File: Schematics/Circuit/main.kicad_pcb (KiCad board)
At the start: 2 copper layers, 58.9 x 59 mm, 103 parts, among them IC1 NCP1117ST33T3G, IC2 NCP1117ST50T3G, IC3 ATMEGA2560-A, IC4 RFM69HW, J1 Conn_01x03, J10 Conn_01x04, J11 Conn_01x04, J12 Conn_01x01, J13 Conn_01x02, J14 Conn_01x02, J15 Conn_01x02, J16 Conn_01x02, J2 Conn_01x07, J3 Conn_01x07, J4 Conn_01x07, J5 Conn_01x07, J6 Conn_01x07, J7 Conn_01x05, J8 Conn_02x05_Counter_Clockwise, J9 Conn_01x06, K1 HESOP1, K2 HESOP1, P1 CONN_2, P10 CONN_2, P11 CONN_2, P12 CONN_2, P13 CONN_2, P14 CONN_2, P15 CONN_2, P16 CONN_2, P17 CONN_2, P18 CONN_3X2, P19 CONN_O2, P2 CONN_2, P20 CONN_2, P21 CONN_2, P3 CONN_2, P4 CONN_2, P5 CONN_2, P6 CONN_2, P7 CONN_2, P8 CONN_2, P9 CONN_2, Q1 BSS138, Q2 BSS138, Q3 BSS138, Q4 BSS138, Q5 BSS138, Q6 BSS138, SW1 SW_DIP_x01, SW7 SW_DIP_x01

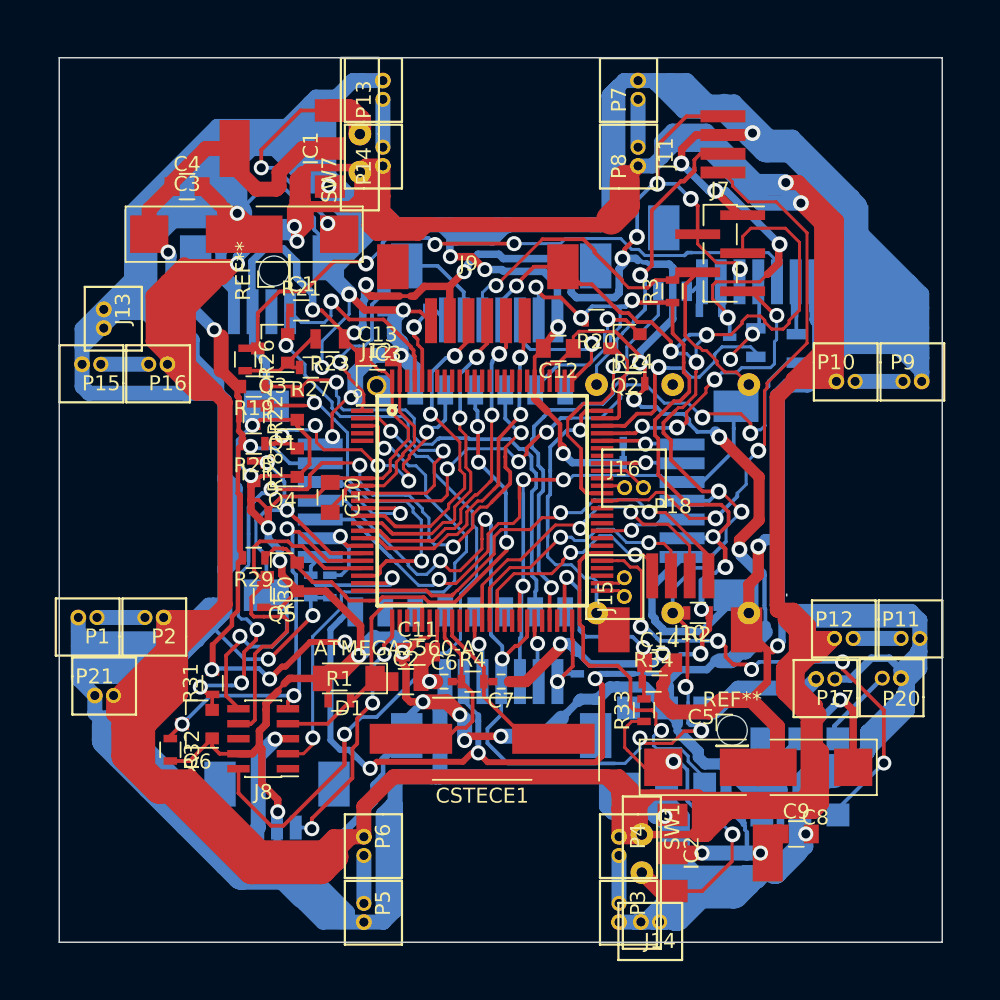
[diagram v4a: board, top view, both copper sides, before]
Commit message: Add UV and Gamma detection, fix main pcb
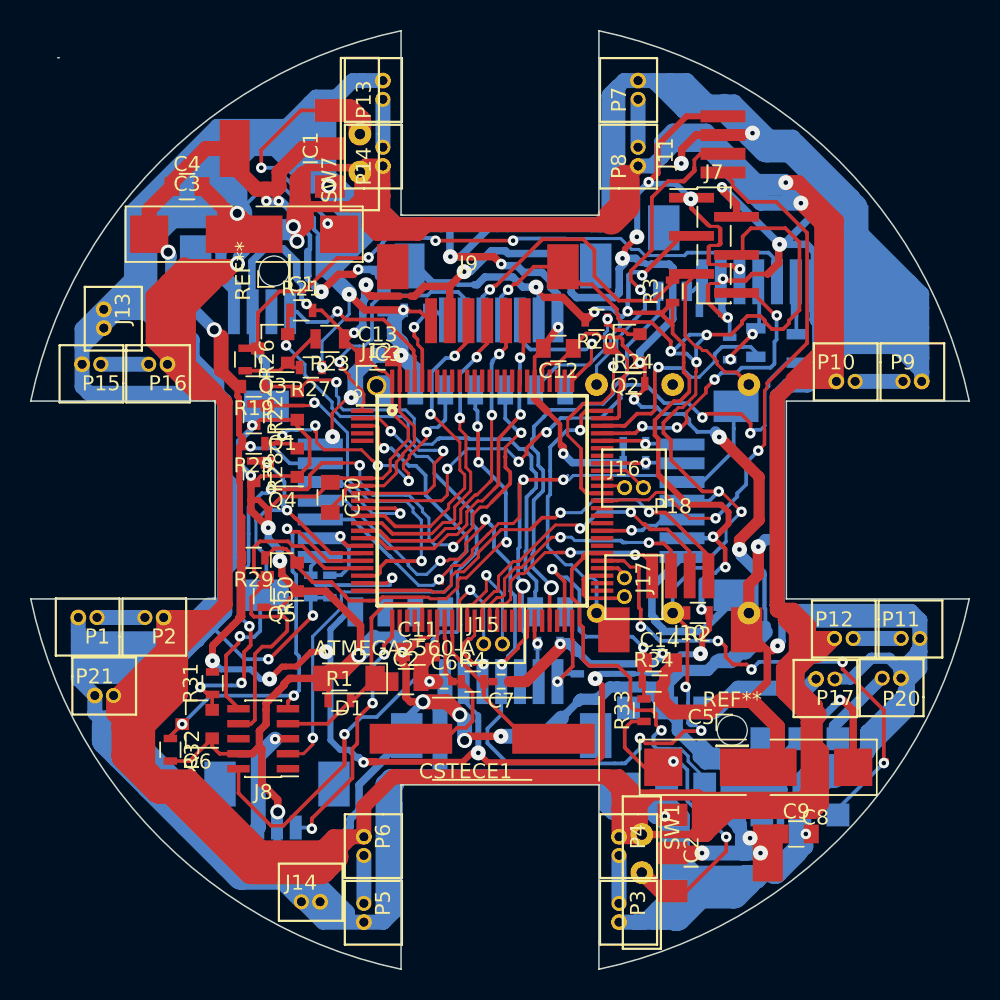
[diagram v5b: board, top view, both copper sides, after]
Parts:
- added J17: Conn_01x02, CanSat:MOLEX_PicoBlade_2, F.Cu at (52.1, 50.6)
- J7: value Conn_01x05 -> Conn_01x06; footprint Pin_Headers:Pin_Header_Straight_1x05_Pitch1.27mm_SMD_Pin1Right -> Pin_Headers:Pin_Header_Straight_1x06_Pitch1.27mm_SMD_Pin1Left
- moved J14 21.4 mm to (31.8, 71.0), turned to 180 degrees
- moved J15 9.26 mm to (44.0, 53.8), turned to 180 degrees
- moved J7 0.66 mm to (58.1, 27.2)
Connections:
- IC3 pad 27: (no net) -> Net-(IC3-Pad27)
- IC3 pad 28: (no net) -> Net-(IC3-Pad28)
- IC3 pad 29: (no net) -> Net-(IC3-Pad29)
- IC3 pad 35: (no net) -> Net-(IC3-Pad35)
- IC3 pad 36: (no net) -> Net-(IC3-Pad36)
- IC3 pad 4: (no net) -> Net-(IC3-Pad4)
- IC3 pad 41: (no net) -> Net-(IC3-Pad41)
- IC3 pad 42: (no net) -> Net-(IC3-Pad42)
- IC3 pad 46: (no net) -> Net-(IC3-Pad46)
- IC3 pad 48: (no net) -> Net-(IC3-Pad48)
- IC3 pad 5: (no net) -> Net-(IC3-Pad5)
- IC3 pad 53: (no net) -> Net-(IC3-Pad53)
- IC3 pad 54: (no net) -> Net-(IC3-Pad54)
- IC3 pad 57: (no net) -> Net-(IC3-Pad57)
- IC3 pad 58: (no net) -> Net-(IC3-Pad58)
- IC3 pad 60: (no net) -> Net-(IC3-Pad60)
- IC3 pad 66: (no net) -> Net-(IC3-Pad66)
- IC3 pad 69: (no net) -> Net-(IC3-Pad69)
- IC3 pad 70: (no net) -> Net-(IC3-Pad70)
- IC3 pad 77: (no net) -> Net-(IC3-Pad77)
- IC3 pad 78: (no net) -> Net-(IC3-Pad78)
- IC3 pad 79: (no net) -> Net-(IC3-Pad79)
- IC3 pad 82: (no net) -> Net-(IC3-Pad82)
- IC3 pad 83: (no net) -> Net-(IC3-Pad83)
- IC3 pad 84: (no net) -> Net-(IC3-Pad84)
- IC3 pad 85: (no net) -> Net-(IC3-Pad85)
- IC3 pad 86: (no net) -> Net-(IC3-Pad86)
- IC3 pad 87: (no net) -> Net-(IC3-Pad87)
- IC3 pad 88: (no net) -> Net-(IC3-Pad88)
- IC3 pad 89: (no net) -> Net-(IC3-Pad89)
- IC3 pad 90: (no net) -> Net-(IC3-Pad90)
- IC3 pad 91: (no net) -> Net-(IC3-Pad91)
- IC3 pad 92: (no net) -> Net-(IC3-Pad92)
- IC3 pad 93: (no net) -> Net-(IC3-Pad93)
- IC3 pad 94: (no net) -> Net-(IC3-Pad94)
- IC3 pad 95: (no net) -> Net-(IC3-Pad95)
- IC3 pad 98: (no net) -> Net-(IC3-Pad98)
- IC4 pad 1: (no net) -> Net-(IC4-Pad1)
- IC4 pad 16: (no net) -> Net-(IC4-Pad16)
- IC4 pad 5: (no net) -> Net-(IC4-Pad5)
- IC4 pad 6: (no net) -> Net-(IC4-Pad6)
- IC4 pad 7: (no net) -> Net-(IC4-Pad7)
- J15 pad 1: Net-(IC3-Pad52) -> Net-(IC3-Pad36)
- J15 pad 2: Net-(IC3-Pad51) -> Net-(IC3-Pad35)
- J5 pad : /INT2 -> +3V3
- J7 pad 1: GND -> +5V
- J7 pad 2: +5V -> GND
- J7 pad 3: /SCL -> +3V3
- J7 pad 4: /SDA -> /SCL
- J7 pad 5: /LED_TOP -> /SDA
- J8 pad 1: (no net) -> /DTR
- J8 pad 6: (no net) -> Net-(J8-Pad6)
- K1 pad 3: (no net) -> Net-(K1-Pad3)
- K1 pad 4: (no net) -> Net-(K1-Pad4)
- K2 pad 3: (no net) -> Net-(K2-Pad3)
- K2 pad 4: (no net) -> Net-(K2-Pad4)
- P18 pad 4: (no net) -> Net-(P18-Pad4)
- P19 pad 3: (no net) -> Net-(P19-Pad3)
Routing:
- net +3V3: track 176.4 -> 222.4 mm, vias 16 -> 21
- net +5V: track 320.5 -> 335.2 mm, vias 27 -> 28
- net GND: track 968.5 -> 982.1 mm, vias 27 -> 28
- net Net-(IC3-Pad36): track 0.00 -> 8.71 mm, vias 0 -> 1
- net Net-(IC3-Pad35): track 0.00 -> 6.32 mm, vias 0 -> 1
- net Net-(IC3-Pad53): track 0.00 -> 5.24 mm
- net /SCK: track 31.5 -> 28.8 mm
- net /LED1: track 4.32 -> 6.65 mm
- net /V_READ: track 15.2 -> 17.2 mm
- net Net-(IC3-Pad54): track 0.00 -> 1.88 mm
- net /SDA: track 90.8 -> 92.5 mm
- net Net-(IC3-Pad51): track 1.64 -> 0.00 mm
- net Net-(IC3-Pad52): track 1.64 -> 0.00 mm
- net /INT2: track 19.6 -> 18.1 mm
- net /LED4: track 5.65 -> 7.04 mm
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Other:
- board size 58.9 x 59 mm -> 62.6 x 62.6 mm
- net class Default: via_dia 1.006 -> 0.706; via_drill 0.6 -> 0.3
- rule via_min_drill: 0.6 -> 0.3
- rule via_min_size: 1.006 -> 0.7
